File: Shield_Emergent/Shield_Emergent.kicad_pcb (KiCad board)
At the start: 2 copper layers, 17 parts, among them J1 Conn_01x02_Female, J2 Conn_01x04_Male, J3 Conn_01x02_Female, J4 Conn_01x04_Male, U1 Raspberri_Pi_Pico, U2 TPS2553, U3 TPS2553

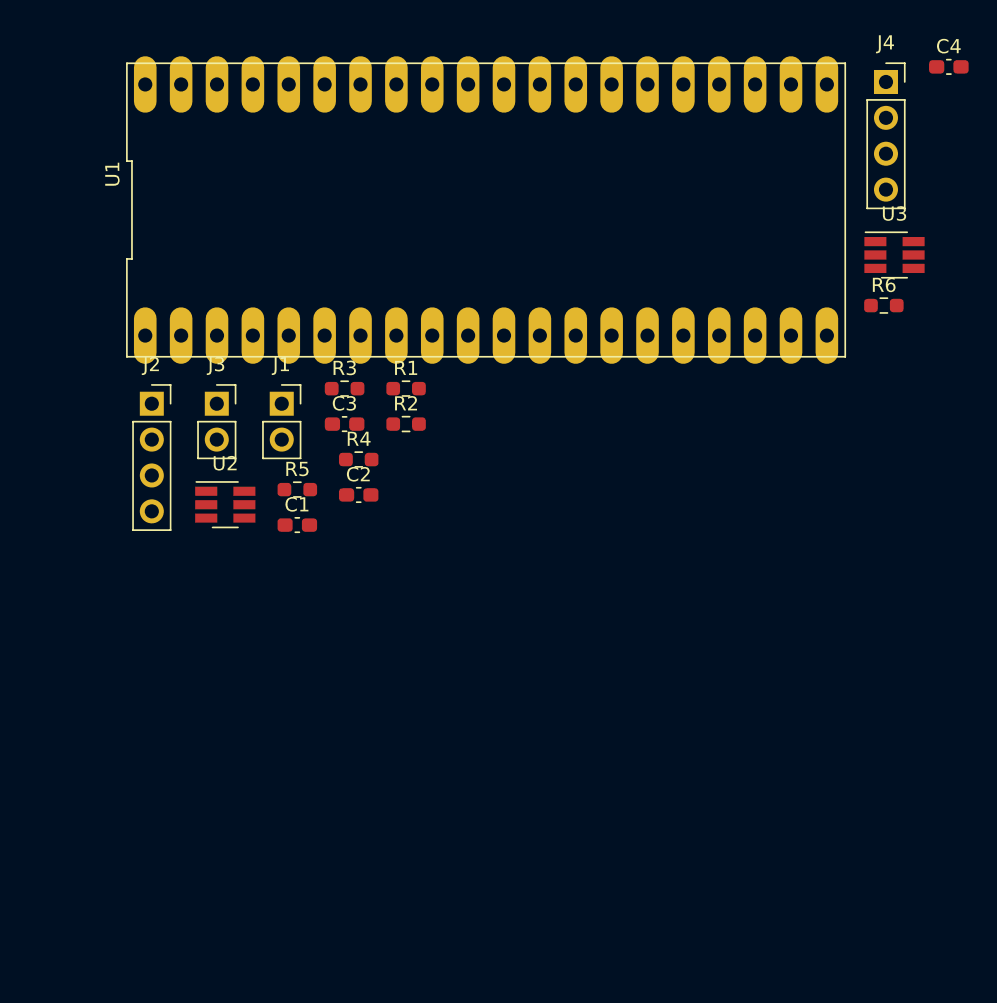
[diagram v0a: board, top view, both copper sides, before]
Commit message: м PCB proto has been created
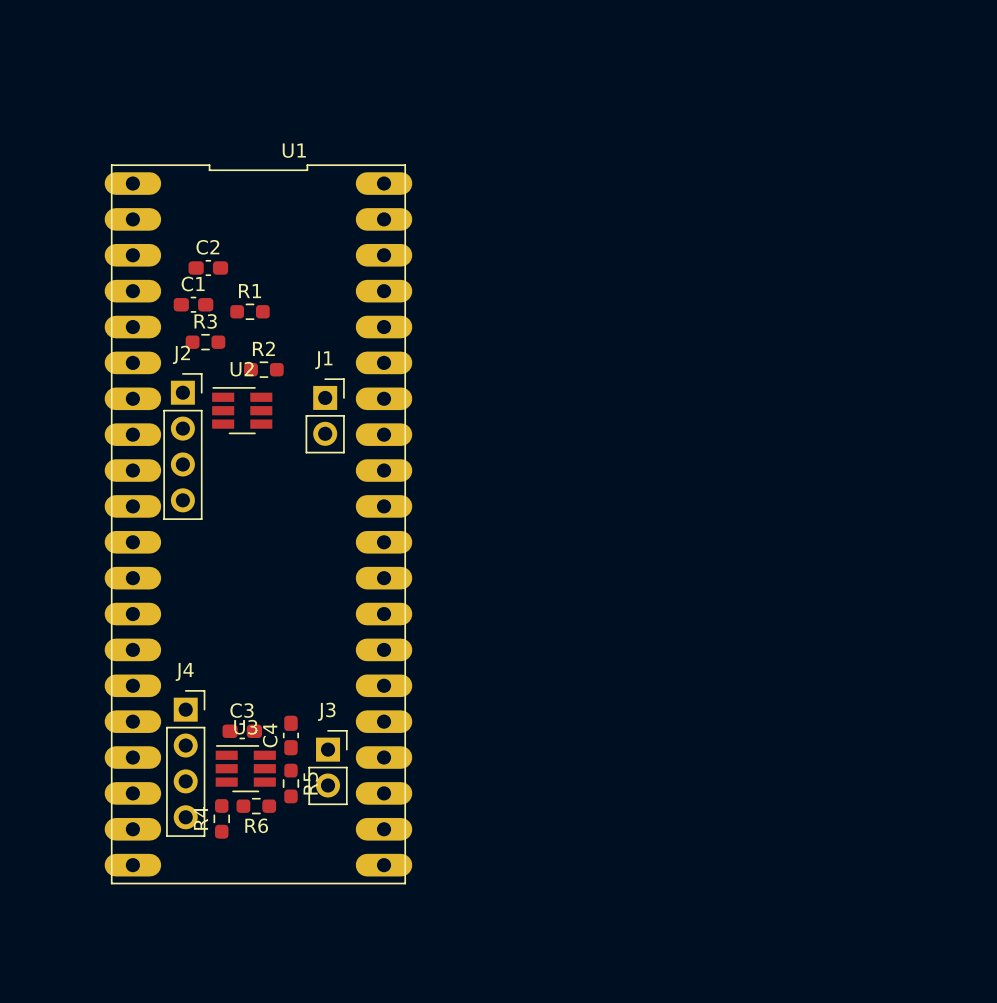
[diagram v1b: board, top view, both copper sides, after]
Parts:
- moved J4 66.6 mm to (32.5, 65.9)
- moved C4 66.4 mm to (40.0, 67.7), turned to 90 degrees
- moved U3 58.6 mm to (36.8, 70.0)
- moved R6 56.8 mm to (37.5, 72.7), turned to 180 degrees
- moved U1 27.5 mm to (37.6, 52.8), turned to -90 degrees
- moved R4 27.2 mm to (35.0, 73.6), turned to 90 degrees
- moved J3 25.7 mm to (42.6, 68.7)
- moved C3 22.9 mm to (36.5, 67.4)
- moved R5 20.8 mm to (40.0, 71.1), turned to -90 degrees
- moved C2 19.3 mm to (34.1, 34.6)
- moved C1 17.2 mm to (33.0, 37.2)
- moved R1 12.3 mm to (37.0, 37.7)
- moved R2 10.8 mm to (38.0, 41.8)
- moved R3 10.4 mm to (33.9, 39.9)
- moved U2 6.77 mm to (36.5, 44.7)
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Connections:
- U2 pad 1: (no net) -> VBUS
- U2 pad 2: (no net) -> GND
- U2 pad 3: (no net) -> EN1
- U2 pad 4: (no net) -> FLT1
- U2 pad 5: (no net) -> Net-(R2-Pad1)
- U2 pad 6: (no net) -> Net-(C2-Pad1)
- U3 pad 1: (no net) -> VBUS
- U3 pad 2: (no net) -> GND
- U3 pad 3: (no net) -> EN2
- U3 pad 4: (no net) -> FLT2
- U3 pad 5: (no net) -> Net-(R5-Pad1)
- U3 pad 6: (no net) -> Net-(C4-Pad1)

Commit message: v0.5 Partial decompoition has been completed
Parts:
- moved R1 10.9 mm to (35.1, 48.5), turned to 90 degrees
- moved C2 9.80 mm to (40.0, 42.4), turned to 90 degrees
- moved R3 8.49 mm to (37.5, 47.5), turned to 180 degrees
- moved C1 5.89 mm to (36.0, 42.3)
- moved R2 4.47 mm to (40.0, 45.8), turned to -90 degrees
- moved U2 0.37 mm to (36.8, 44.9)
- moved J1 0.25 mm to (42.6, 43.8)
- moved J2 0.25 mm to (32.5, 43.5)
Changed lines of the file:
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@@
   )
   (footprint "Capacitor_SMD:C_0603_1608Metric_Pad1.08x0.95mm_HandSolder" (layer "F.Cu")
-    (at 34.1 34.6)
+    (at 40 42.42 90)
     (descr "Capacitor SMD 0603 (1608 Metric), square (rectangular) end terminal, IPC_7351 nominal with elongated pad for handsoldering. (Body size source: IPC-SM-782 page 76, https://www.pcb-3d.com/wordpress/wp-content/uploads/ipc-sm-782a_amendment_1_and_2.pdf), generated with kicad-footprint-generator")
     (tags "capacitor handsolder")
@@
     (property "Sheetname" "")
     (attr smd)
-    (fp_text reference "C2" (at 0 -1.43) (layer "F.SilkS")
-      (effects (font (size 1 1) (thickness 0.15)))
-    )
-    (fp_text value "2.2" (at 0 1.43) (layer "F.Fab")
-      (effects (font (size 1 1) (thickness 0.15)))
-    )
-    (fp_text user "${REFERENCE}" (at 0 0) (layer "F.Fab")
+    (fp_text reference "C2" (at 0 -1.43 90) (layer "F.SilkS")
+      (effects (font (size 1 1) (thickness 0.15)))
+    )
+    (fp_text value "2.2" (at 0 1.43 90) (layer "F.Fab")
+      (effects (font (size 1 1) (thickness 0.15)))
+    )
+    (fp_text user "${REFERENCE}" (at 0 0 90) (layer "F.Fab")
       (effects (font (size 0.4 0.4) (thickness 0.06)))
     )
@@
     (fp_line (start 0.8 0.4) (end -0.8 0.4) (layer "F.Fab") (width 0.1))
     (fp_line (start 0.8 -0.4) (end 0.8 0.4) (layer "F.Fab") (width 0.1))
-    (pad "1" smd roundrect (at -0.8625 0) (size 1.075 0.95) (layers "F.Cu" "F.Paste" "F.Mask") (roundrect_rratio 0.25)
+    (pad "1" smd roundrect (at -0.8625 0 90) (size 1.075 0.95) (layers "F.Cu" "F.Paste" "F.Mask") (roundrect_rratio 0.25)
       (net 3 "Net-(C2-Pad1)") (pintype "passive"))
-    (pad "2" smd roundrect (at 0.8625 0) (size 1.075 0.95) (layers "F.Cu" "F.Paste" "F.Mask") (roundrect_rratio 0.25)
+    (pad "2" smd roundrect (at 0.8625 0 90) (size 1.075 0.95) (layers "F.Cu" "F.Paste" "F.Mask") (roundrect_rratio 0.25)
       (net 2 "GND") (pintype "passive"))
     (model "${KICAD6_3DMODEL_DIR}/Capacitor_SMD.3dshapes/C_0603_1608Metric.wrl"
@@
   )
   (footprint "Resistor_SMD:R_0603_1608Metric_Pad0.98x0.95mm_HandSolder" (layer "F.Cu")
-    (at 38.0375 41.8)
+    (at 40 45.82 -90)
     (descr "Resistor SMD 0603 (1608 Metric), square (rectangular) end terminal, IPC_7351 nominal with elongated pad for handsoldering. (Body size source: IPC-SM-782 page 72, https://www.pcb-3d.com/wordpress/wp-content/uploads/ipc-sm-782a_amendment_1_and_2.pdf), generated with kicad-footprint-generator")
     (tags "resistor handsolder")
@@
     (property "Sheetname" "")
     (attr smd)
-    (fp_text reference "R2" (at 0 -1.43) (layer "F.SilkS")
-      (effects (font (size 1 1) (thickness 0.15)))
-    )
-    (fp_text value "R" (at 0 1.43) (layer "F.Fab")
-      (effects (font (size 1 1) (thickness 0.15)))
-    )
-    (fp_text user "${REFERENCE}" (at 0 0) (layer "F.Fab")
+    (fp_text reference "R2" (at 0 -1.43 90) (layer "F.SilkS")
+      (effects (font (size 1 1) (thickness 0.15)))
+    )
+    (fp_text value "R" (at 0 1.43 90) (layer "F.Fab")
+      (effects (font (size 1 1) (thickness 0.15)))
+    )
+    (fp_text user "${REFERENCE}" (at 0 0 90) (layer "F.Fab")
       (effects (font (size 0.4 0.4) (thickness 0.06)))
     )
@@
     (fp_line (start -0.8 -0.4125) (end 0.8 -0.4125) (layer "F.Fab") (width 0.1))
     (fp_line (start 0.8 -0.4125) (end 0.8 0.4125) (layer "F.Fab") (width 0.1))
-    (pad "1" smd roundrect (at -0.9125 0) (size 0.975 0.95) (layers "F.Cu" "F.Paste" "F.Mask") (roundrect_rratio 0.25)
+    (pad "1" smd roundrect (at -0.9125 0 270) (size 0.975 0.95) (layers "F.Cu" "F.Paste" "F.Mask") (roundrect_rratio 0.25)
       (net 9 "Net-(R2-Pad1)") (pintype "passive"))
-    (pad "2" smd roundrect (at 0.9125 0) (size 0.975 0.95) (layers "F.Cu" "F.Paste" "F.Mask") (roundrect_rratio 0.25)
+    (pad "2" smd roundrect (at 0.9125 0 270) (size 0.975 0.95) (layers "F.Cu" "F.Paste" "F.Mask") (roundrect_rratio 0.25)
       (net 2 "GND") (pintype "passive"))
     (model "${KICAD6_3DMODEL_DIR}/Resistor_SMD.3dshapes/R_0603_1608Metric.wrl"
@@
       (effects (font (size 1 1) (thickness 0.15)))
     )
-    (fp_text value "Raspberri_Pi_Pico" (at 0 0 90) (layer "F.Fab")
+    (fp_text value "Raspberri_Pi_Pico" (at 0.02 -0.25 90) (layer "F.Fab")
       (effects (font (size 1 1) (thickness 0.15)))
     )
@@
   )
   (footprint "Connector_PinSocket_2.54mm:PinSocket_1x04_P2.54mm_Vertical" (layer "F.Cu")
-    (at 32.3 43.43)
+    (at 32.55 43.45)
     (descr "Through hole straight socket strip, 1x04, 2.54mm pitch, single row (from Kicad 4.0.7), script generated")
     (tags "Through hole socket strip THT 1x04 2.54mm single row")
@@
   )
   (footprint "Resistor_SMD:R_0603_1608Metric_Pad0.98x0.95mm_HandSolder" (layer "F.Cu")
-    (at 37.05 37.7)
+    (at 35.1 48.47 90)
     (descr "Resistor SMD 0603 (1608 Metric), square (rectangular) end terminal, IPC_7351 nominal with elongated pad for handsoldering. (Body size source: IPC-SM-782 page 72, https://www.pcb-3d.com/wordpress/wp-content/uploads/ipc-sm-782a_amendment_1_and_2.pdf), generated with kicad-footprint-generator")
     (tags "resistor handsolder")
@@
     (property "Sheetname" "")
     (attr smd)
-    (fp_text reference "R1" (at 0 -1.43) (layer "F.SilkS")
-      (effects (font (size 1 1) (thickness 0.15)))
-    )
-    (fp_text value "10k" (at 0 1.43) (layer "F.Fab")
-      (effects (font (size 1 1) (thickness 0.15)))
-    )
-    (fp_text user "${REFERENCE}" (at 0 0) (layer "F.Fab")
+    (fp_text reference "R1" (at 0 -1.43 90) (layer "F.SilkS")
+      (effects (font (size 1 1) (thickness 0.15)))
+    )
+    (fp_text value "10k" (at 0 1.43 90) (layer "F.Fab")
+      (effects (font (size 1 1) (thickness 0.15)))
+    )
+    (fp_text user "${REFERENCE}" (at 0 0 90) (layer "F.Fab")
       (effects (font (size 0.4 0.4) (thickness 0.06)))
     )
@@
     (fp_line (start -0.8 -0.4125) (end 0.8 -0.4125) (layer "F.Fab") (width 0.1))
     (fp_line (start 0.8 0.4125) (end -0.8 0.4125) (layer "F.Fab") (width 0.1))
-    (pad "1" smd roundrect (at -0.9125 0) (size 0.975 0.95) (layers "F.Cu" "F.Paste" "F.Mask") (roundrect_rratio 0.25)
+    (pad "1" smd roundrect (at -0.9125 0 90) (size 0.975 0.95) (layers "F.Cu" "F.Paste" "F.Mask") (roundrect_rratio 0.25)
       (net 1 "VBUS") (pintype "passive"))
-    (pad "2" smd roundrect (at 0.9125 0) (size 0.975 0.95) (layers "F.Cu" "F.Paste" "F.Mask") (roundrect_rratio 0.25)
+    (pad "2" smd roundrect (at 0.9125 0 90) (size 0.975 0.95) (layers "F.Cu" "F.Paste" "F.Mask") (roundrect_rratio 0.25)
       (net 5 "EN1") (pintype "passive"))
     (model "${KICAD6_3DMODEL_DIR}/Resistor_SMD.3dshapes/R_0603_1608Metric.wrl"
@@
   )
   (footprint "Resistor_SMD:R_0603_1608Metric_Pad0.98x0.95mm_HandSolder" (layer "F.Cu")
-    (at 33.9 39.85)
+    (at 37.55 47.52 180)
     (descr "Resistor SMD 0603 (1608 Metric), square (rectangular) end terminal, IPC_7351 nominal with elongated pad for handsoldering. (Body size source: IPC-SM-782 page 72, https://www.pcb-3d.com/wordpress/wp-content/uploads/ipc-sm-782a_amendment_1_and_2.pdf), generated with kicad-footprint-generator")
     (tags "resistor handsolder")
@@
     (fp_line (start 0.8 -0.4125) (end 0.8 0.4125) (layer "F.Fab") (width 0.1))
     (fp_line (start -0.8 0.4125) (end -0.8 -0.4125) (layer "F.Fab") (width 0.1))
-    (pad "1" smd roundrect (at -0.9125 0) (size 0.975 0.95) (layers "F.Cu" "F.Paste" "F.Mask") (roundrect_rratio 0.25)
+    (pad "1" smd roundrect (at -0.9125 0 180) (size 0.975 0.95) (layers "F.Cu" "F.Paste" "F.Mask") (roundrect_rratio 0.25)
       (net 6 "FLT1") (pintype "passive"))
-    (pad "2" smd roundrect (at 0.9125 0) (size 0.975 0.95) (layers "F.Cu" "F.Paste" "F.Mask") (roundrect_rratio 0.25)
+    (pad "2" smd roundrect (at 0.9125 0 180) (size 0.975 0.95) (layers "F.Cu" "F.Paste" "F.Mask") (roundrect_rratio 0.25)
       (net 1 "VBUS") (pintype "passive"))
     (model "${KICAD6_3DMODEL_DIR}/Resistor_SMD.3dshapes/R_0603_1608Metric.wrl"
@@
   )
   (footprint "Package_TO_SOT_SMD:SOT-23-6_Handsoldering" (layer "F.Cu")
-    (at 36.5 44.7)
+    (at 36.8 44.92)
     (descr "6-pin SOT-23 package, Handsoldering")
     (tags "SOT-23-6 Handsoldering")
@@
   )
   (footprint "Capacitor_SMD:C_0603_1608Metric_Pad1.08x0.95mm_HandSolder" (layer "F.Cu")
-    (at 33.05 37.2)
+    (at 36.05 42.27)
     (descr "Capacitor SMD 0603 (1608 Metric), square (rectangular) end terminal, IPC_7351 nominal with elongated pad for handsoldering. (Body size source: IPC-SM-782 page 76, https://www.pcb-3d.com/wordpress/wp-content/uploads/ipc-sm-782a_amendment_1_and_2.pdf), generated with kicad-footprint-generator")
     (tags "capacitor handsolder")
@@
   )
   (footprint "Connector_PinSocket_2.54mm:PinSocket_1x02_P2.54mm_Vertical" (layer "F.Cu")
-    (at 42.375 43.8)
+    (at 42.625 43.82)
     (descr "Through hole straight socket strip, 1x02, 2.54mm pitch, single row (from Kicad 4.0.7), script generated")
     (tags "Through hole socket strip THT 1x02 2.54mm single row")

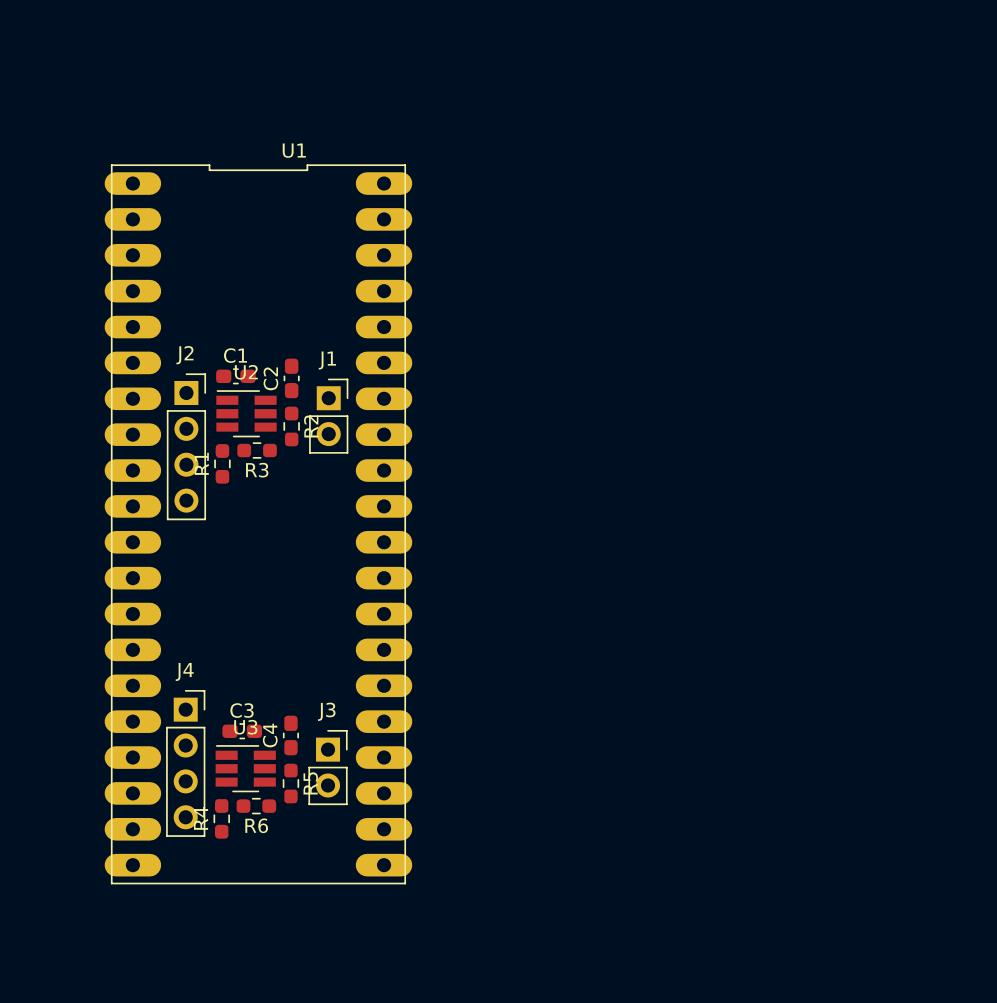
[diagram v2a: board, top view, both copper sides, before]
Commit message: v0.6 partially routed
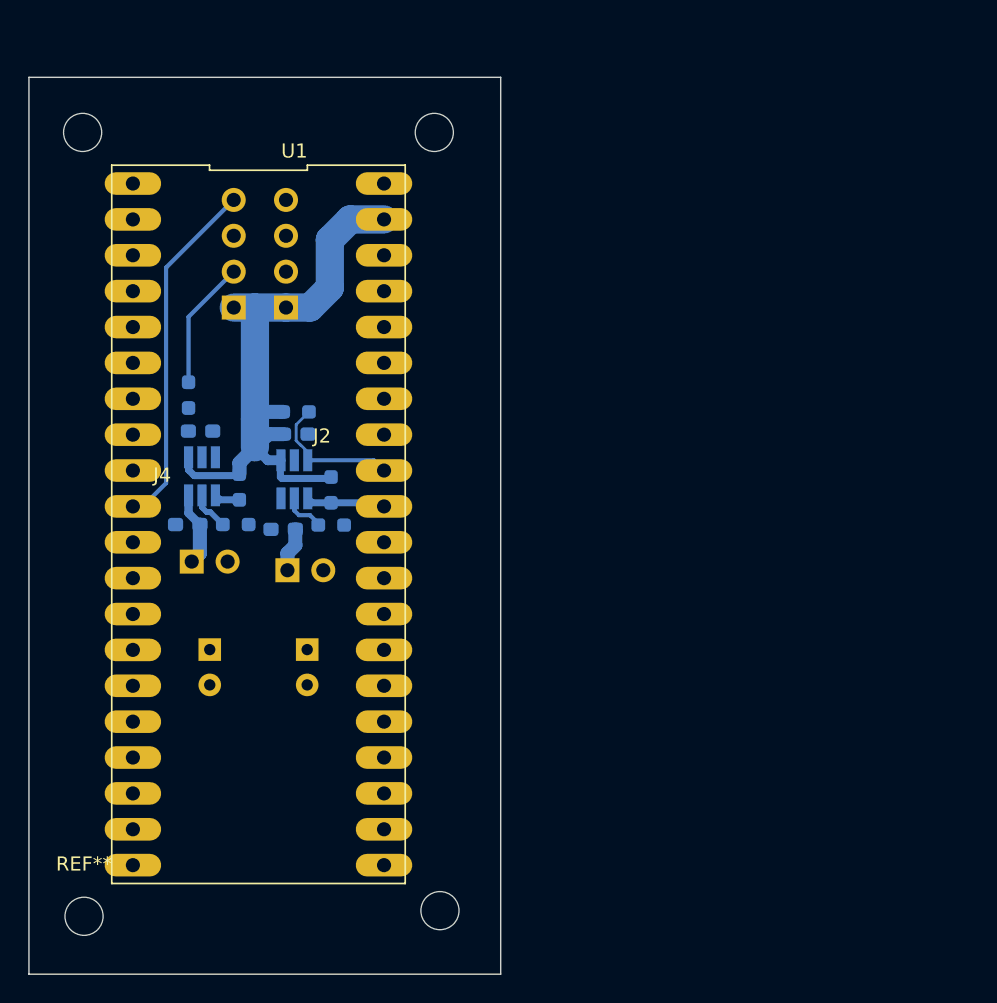
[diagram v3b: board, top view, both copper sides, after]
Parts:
- added C3: 120 uF, Capacitor_THT:CP_Radial_D6.3mm_P2.50mm, B.Cu at (41.1, 61.6)
- added C6: 120 uF, Capacitor_THT:CP_Radial_D6.3mm_P2.50mm, B.Cu at (34.2, 61.6)
- added REF**: MountingHole_2.7mm_M2.5, MountingHole:MountingHole_2.7mm_M2.5, F.Cu at (50.5, 80.1)
- added REF**: MountingHole_2.7mm_M2.5, MountingHole:MountingHole_2.7mm_M2.5, F.Cu at (25.3, 80.5)
- added REF**: MountingHole_2.7mm_M2.5, MountingHole:MountingHole_2.7mm_M2.5, F.Cu at (25.2, 25.0)
- added REF**: MountingHole_2.7mm_M2.5, MountingHole:MountingHole_2.7mm_M2.5, F.Cu at (50.1, 25.0)
- C1, C2, J1, J2, J3, J4, R1, R2, R3, R4, R5, R6, U2, U3: moved to B.Cu
- C4: renamed from C3; moved to B.Cu
- C5: renamed from C4; moved to B.Cu
- moved R4 30.1 mm to (32.7, 43.6)
- moved J4 28.7 mm to (35.9, 37.4)
- moved R6 22.6 mm to (36.3, 50.1), turned to 90 degrees
- moved C4 21.5 mm to (33.5, 46.1)
- moved U3 20.9 mm to (33.6, 49.4), turned to -90 degrees
- moved R5 18.7 mm to (36.0, 52.8), turned to 0 degrees
- moved C5 16.6 mm to (32.6, 52.8), turned to 180 degrees
- moved J3 16.4 mm to (32.9, 55.4), turned to -90 degrees
- moved J1 12.5 mm to (39.7, 56.0), turned to -90 degrees
- moved C2 10.7 mm to (39.4, 53.1), turned to 180 degrees
- moved J2 9.29 mm to (39.6, 37.4)
- moved R2 7.52 mm to (42.8, 52.8), turned to 0 degrees
- moved R1 6.38 mm to (40.3, 44.8), turned to 0 degrees
- moved R3 5.94 mm to (42.8, 50.3), turned to 90 degrees
- moved C1 5.89 mm to (40.3, 46.4)
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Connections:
- U1 pad 10: unconnected-(U1-Pad10) -> FLT2
- U1 pad 31: unconnected-(U1-Pad31) -> FLT1
- U1 pad 32: unconnected-(U1-Pad32) -> EN1
- U1 pad 9: unconnected-(U1-Pad9) -> EN2
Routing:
- net VBUS: track 0.00 -> 43.3 mm
- net FLT2: track 0.00 -> 26.9 mm
- net EN1: track 0.00 -> 9.86 mm
- net EN2: track 0.00 -> 9.15 mm
- net FLT1: track 0.00 -> 5.64 mm
- net Net-(C5-Pad1): track 0.00 -> 5.26 mm
- net Net-(C2-Pad1): track 0.00 -> 3.13 mm
- net Net-(R2-Pad1): track 0.00 -> 3.05 mm
- net Net-(R5-Pad1): track 0.00 -> 2.83 mm
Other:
- board outline added: 33.4 x 63.5 mm

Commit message: v0.7 Routing has been completed
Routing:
- net FLT1: track 5.64 -> 29.6 mm, vias 0 -> 1
- net EN1: track 9.86 -> 29.3 mm, vias 0 -> 1
- net EN2: track 9.15 -> 23.6 mm
- net Net-(C2-Pad1): track 3.13 -> 11.9 mm
- net GND: track 0.00 -> 8.56 mm, vias 0 -> 43
- net FLT2: track 26.9 -> 35.4 mm, vias 0 -> 1
- net VBUS: track 43.3 -> 50.6 mm
- net Net-(C5-Pad1): track 5.26 -> 12.0 mm
- added copper zone on B.Cu, net GND
- added copper zone on F.Cu, net GND
